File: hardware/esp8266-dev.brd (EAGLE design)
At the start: 48.3 x 48.3 mm, 31 parts, among them CON1 USBB-SOCKET

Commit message: first acceptable layout, off to review
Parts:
- added U$3: (no value), p.peter-doc:LOGO-JUSTGEEK-XXXS
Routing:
- net +3V3: track 115.8 -> 116.6 mm
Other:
- board text added: "+3V3"
- board text added: "0"
- board text added: "16"
- board text added: "2"
- board text added: "GND"
- board text added: "ISP 3v3"
- board text added: "RX"
- board text added: "TX"
- board text added: "github.com/JustgeekDE/ESP8266-devBoard"
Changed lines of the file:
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@@
 <setting verticaltext="up"/>
 </settings>
-<grid distance="0.05" unitdist="inch" unit="mil" style="lines" multiple="1" display="yes" altdistance="10" altunitdist="mil" altunit="mil"/>
+<grid distance="10" unitdist="mil" unit="mil" style="lines" multiple="1" display="yes" altdistance="5" altunitdist="mil" altunit="mil"/>
 <layers>
 <layer number="1" name="Top" color="4" fill="1" visible="no" active="yes"/>
@@
 <layer number="19" name="Unrouted" color="6" fill="1" visible="no" active="yes"/>
 <layer number="20" name="Dimension" color="15" fill="1" visible="yes" active="yes"/>
-<layer number="21" name="tPlace" color="7" fill="1" visible="yes" active="yes"/>
-<layer number="22" name="bPlace" color="7" fill="1" visible="no" active="yes"/>
+<layer number="21" name="tPlace" color="7" fill="1" visible="no" active="yes"/>
+<layer number="22" name="bPlace" color="7" fill="1" visible="yes" active="yes"/>
 <layer number="23" name="tOrigins" color="15" fill="1" visible="no" active="yes"/>
-<layer number="24" name="bOrigins" color="15" fill="1" visible="no" active="yes"/>
-<layer number="25" name="tNames" color="7" fill="1" visible="yes" active="yes"/>
-<layer number="26" name="bNames" color="7" fill="1" visible="no" active="yes"/>
-<layer number="27" name="tValues" color="7" fill="1" visible="yes" active="yes"/>
-<layer number="28" name="bValues" color="7" fill="1" visible="no" active="yes"/>
-<layer number="29" name="tStop" color="7" fill="3" visible="yes" active="yes"/>
-<layer number="30" name="bStop" color="7" fill="6" visible="no" active="yes"/>
+<layer number="24" name="bOrigins" color="15" fill="1" visible="yes" active="yes"/>
+<layer number="25" name="tNames" color="7" fill="1" visible="no" active="yes"/>
+<layer number="26" name="bNames" color="7" fill="1" visible="yes" active="yes"/>
+<layer number="27" name="tValues" color="7" fill="1" visible="no" active="yes"/>
+<layer number="28" name="bValues" color="7" fill="1" visible="yes" active="yes"/>
+<layer number="29" name="tStop" color="7" fill="3" visible="no" active="yes"/>
+<layer number="30" name="bStop" color="7" fill="6" visible="yes" active="yes"/>
 <layer number="31" name="tCream" color="7" fill="4" visible="no" active="yes"/>
 <layer number="32" name="bCream" color="7" fill="5" visible="no" active="yes"/>
@@
 <layer number="110" name="fp0" color="7" fill="1" visible="no" active="yes"/>
 <layer number="116" name="Patch_BOT" color="9" fill="4" visible="no" active="yes"/>
-<layer number="121" name="_tsilk" color="7" fill="1" visible="yes" active="yes"/>
-<layer number="122" name="_bsilk" color="7" fill="1" visible="no" active="yes"/>
+<layer number="121" name="_tsilk" color="7" fill="1" visible="no" active="yes"/>
+<layer number="122" name="_bsilk" color="7" fill="1" visible="yes" active="yes"/>
 <layer number="123" name="tTestmark" color="7" fill="1" visible="no" active="yes"/>
 <layer number="124" name="bTestmark" color="7" fill="1" visible="no" active="yes"/>
@@
 <wire x1="48.26" y1="3.81" x2="48.26" y2="5.08" width="0" layer="20"/>
 <wire x1="46.99" y1="49.53" x2="48.26" y2="48.26" width="0" layer="20" curve="-90"/>
+<text x="31.75" y="45.72" size="1.27" layer="21" font="vector" ratio="12" align="center-left">+3V3</text>
+<text x="31.75" y="43.18" size="1.27" layer="21" font="vector" ratio="12" align="center-left">RX</text>
+<text x="31.75" y="40.64" size="1.27" layer="21" font="vector" ratio="12" align="center-left">TX</text>
+<text x="31.75" y="38.1" size="1.27" layer="21" font="vector" ratio="12" align="center-left">16</text>
+<text x="31.75" y="35.56" size="1.27" layer="21" font="vector" ratio="12" align="center-left">2</text>
+<text x="31.75" y="33.02" size="1.27" layer="21" font="vector" ratio="12" align="center-left">0</text>
+<text x="31.75" y="30.48" size="1.27" layer="21" font="vector" ratio="12" align="center-left">GND</text>
+<wire x1="11.303" y1="45.72" x2="11.557" y2="45.72" width="0.508" layer="21"/>
+<wire x1="13.843" y1="45.72" x2="14.097" y2="45.72" width="0.508" layer="21"/>
+<wire x1="16.383" y1="45.72" x2="16.637" y2="45.72" width="0.508" layer="21"/>
+<wire x1="18.923" y1="45.72" x2="19.177" y2="45.72" width="0.508" layer="21"/>
+<wire x1="21.463" y1="45.72" x2="21.717" y2="45.72" width="0.508" layer="21"/>
+<wire x1="24.003" y1="45.72" x2="24.257" y2="45.72" width="0.508" layer="21"/>
+<wire x1="26.543" y1="45.72" x2="26.797" y2="45.72" width="0.508" layer="21"/>
+<wire x1="29.083" y1="45.72" x2="29.337" y2="45.72" width="0.508" layer="21"/>
+<wire x1="26.543" y1="27.94" x2="26.797" y2="27.94" width="0.508" layer="21"/>
+<wire x1="24.003" y1="27.94" x2="24.257" y2="27.94" width="0.508" layer="21"/>
+<wire x1="21.463" y1="27.94" x2="21.717" y2="27.94" width="0.508" layer="21"/>
+<wire x1="18.923" y1="27.94" x2="19.177" y2="27.94" width="0.508" layer="21"/>
+<wire x1="16.383" y1="27.94" x2="16.637" y2="27.94" width="0.508" layer="21"/>
+<wire x1="13.843" y1="27.94" x2="14.097" y2="27.94" width="0.508" layer="21"/>
+<wire x1="11.303" y1="27.94" x2="11.557" y2="27.94" width="0.508" layer="21"/>
+<wire x1="8.763" y1="27.94" x2="9.017" y2="27.94" width="0.508" layer="21"/>
+<wire x1="6.223" y1="27.94" x2="6.477" y2="27.94" width="0.508" layer="21"/>
+<wire x1="3.683" y1="27.94" x2="3.937" y2="27.94" width="0.508" layer="21"/>
+<wire x1="29.21" y1="27.94" x2="30.48" y2="29.21" width="0.508" layer="21" curve="90"/>
+<wire x1="31.115" y1="22.225" x2="47.625" y2="22.225" width="0.508" layer="21" style="shortdash"/>
+<wire x1="30.988" y1="22.225" x2="47.498" y2="22.225" width="0.508" layer="22" style="shortdash"/>
+<text x="37.592" y="15.748" size="1.016" layer="21" font="vector" ratio="12" rot="SR0" align="center">+3V3</text>
+<text x="31.496" y="17.78" size="1.016" layer="21" font="vector" ratio="12" align="center-right">GND</text>
+<text x="40.64" y="16.256" size="1.016" layer="21" font="vector" ratio="12" rot="SR270" align="center-left">TX</text>
+<text x="43.18" y="16.256" size="1.016" layer="21" font="vector" ratio="12" rot="SR270" align="center-left">RX</text>
+<text x="31.496" y="26.67" size="1.016" layer="21" font="vector" ratio="12" align="center-right">GND</text>
+<text x="37.338" y="28.702" size="1.016" layer="21" font="vector" ratio="12" rot="SR0" align="center">+3V3</text>
+<text x="40.64" y="28.702" size="1.016" layer="21" font="vector" ratio="12" rot="SR0" align="center">TX</text>
+<text x="43.18" y="28.702" size="1.016" layer="21" font="vector" ratio="12" rot="SR0" align="center">RX</text>
+<text x="33.02" y="8.636" size="1.016" layer="22" font="vector" ratio="12" rot="MR0" align="center">ISP
+3v3</text>
+<text x="20.32" y="48.006" size="1.016" layer="22" font="vector" ratio="12" rot="MR0" align="center">github.com/JustgeekDE/ESP8266-devBoard</text>
 </plain>
 <attributes>
@@
 <attribute name="VALUE" x="34.29" y="7.62" size="1.27" layer="27" font="vector" ratio="12" rot="R270" align="center"/>
 </element>
-<element name="SJ1" library="jumper" package="SJ" value="" x="33.02" y="5.08" rot="MR90"/>
+<element name="SJ1" library="jumper" package="SJ" value="" x="33.02" y="5.08" smashed="yes" rot="MR90">
+<attribute name="VALUE" x="33.02" y="5.4801" size="0.02" layer="28" rot="MR90"/>
+</element>
 <element name="CON1" library="p.peter-connectors" package="PN61729-S" value="USBB-SOCKET" x="3.81" y="10.16" smashed="yes" rot="R270"/>
 <element name="RF1" library="p.peter-periphery" package="ESP8266-ESP-01-NOSILK" value="" x="44.45" y="34.29" smashed="yes" rot="R180">
@@
 </element>
 <element name="R4" library="rcl" package="0204/7" value="10k" x="39.37" y="34.29" smashed="yes" rot="R90">
-<attribute name="NAME" x="40.8686" y="30.988" size="1.016" layer="25" font="vector" ratio="12" rot="R90" align="center"/>
+<attribute name="NAME" x="39.3446" y="40.132" size="1.016" layer="25" font="vector" ratio="12" rot="R90" align="center"/>
 <attribute name="VALUE" x="39.3446" y="33.6804" size="1.27" layer="27" font="vector" ratio="12" rot="R90" align="center"/>
 </element>
 <element name="R6" library="rcl" package="0204/7" value="10k" x="36.83" y="34.29" smashed="yes" rot="R90">
-<attribute name="NAME" x="34.7726" y="30.988" size="1.016" layer="25" font="vector" ratio="12" rot="R90" align="center"/>
+<attribute name="NAME" x="36.8046" y="40.132" size="1.016" layer="25" font="vector" ratio="12" rot="R90" align="center"/>
 <attribute name="VALUE" x="36.8046" y="33.6804" size="1.27" layer="27" font="vector" ratio="12" rot="R90" align="center"/>
 </element>
@@
 <element name="CON10" library="p.peter-connectors" package="PINHEADER-100MIL-1X7-NOSILK" value="" x="30.48" y="38.1" smashed="yes" rot="R270"/>
 <element name="CON3" library="p.peter-connectors" package="PINHEADER-100MIL-1X8-NOSILK" value="" x="19.05" y="43.18" smashed="yes"/>
+<element name="U$3" library="p.peter-doc" package="LOGO-JUSTGEEK-XXXS" value="" x="43.434" y="45.974" rot="MR0"/>
 </elements>
 <signals>
@@
 <wire x1="38.1" y1="17.78" x2="38.1" y2="26.67" width="0.508" layer="1"/>
 <wire x1="36.83" y1="11.43" x2="34.29" y2="11.43" width="0.508" layer="1"/>
-<wire x1="34.29" y1="11.43" x2="33.02" y2="10.16" width="0.508" layer="1"/>
-<wire x1="33.02" y1="10.16" x2="33.02" y2="9.144" width="0.508" layer="1"/>
-<via x="33.02" y="9.144" extent="1-16" drill="0.508"/>
-<wire x1="33.02" y1="9.144" x2="33.02" y2="5.842" width="0.508" layer="16"/>
+<wire x1="34.29" y1="11.43" x2="33.02" y2="11.43" width="0.508" layer="1"/>
+<via x="33.02" y="11.43" extent="1-16" drill="0.508"/>
+<wire x1="33.02" y1="11.43" x2="33.02" y2="5.842" width="0.508" layer="16"/>
 <contactref element="RF1" pad="VCC"/>
 <contactref element="R4" pad="2"/>
@@
 </board>
 </drawing>
+<compatibility>
+<note version="6.3" minversion="6.2.2" severity="warning">
+Since Version 6.2.2 text objects can contain more than one line,
+which will not be processed correctly with this version.
+</note>
+</compatibility>
 </eagle>

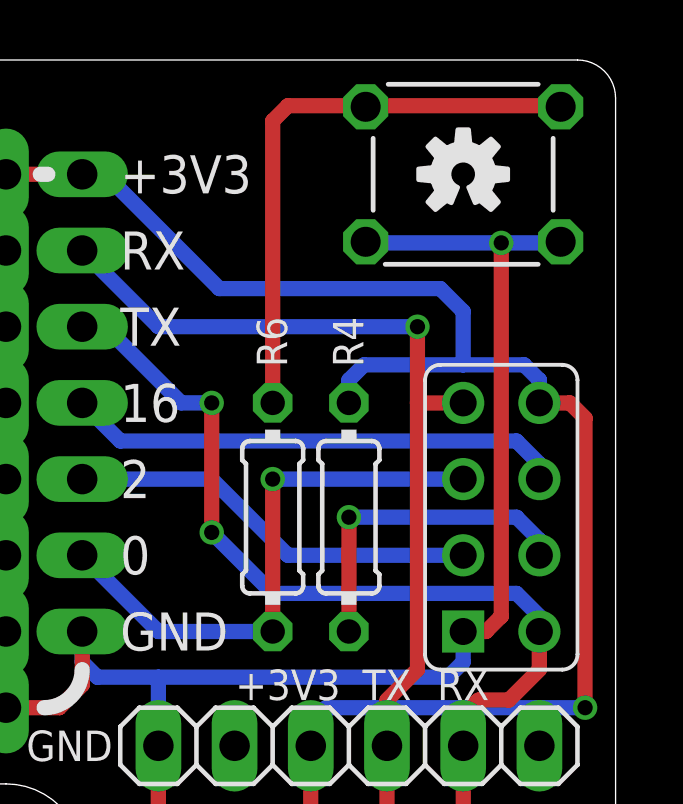
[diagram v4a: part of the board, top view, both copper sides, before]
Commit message: Added more silkscreen
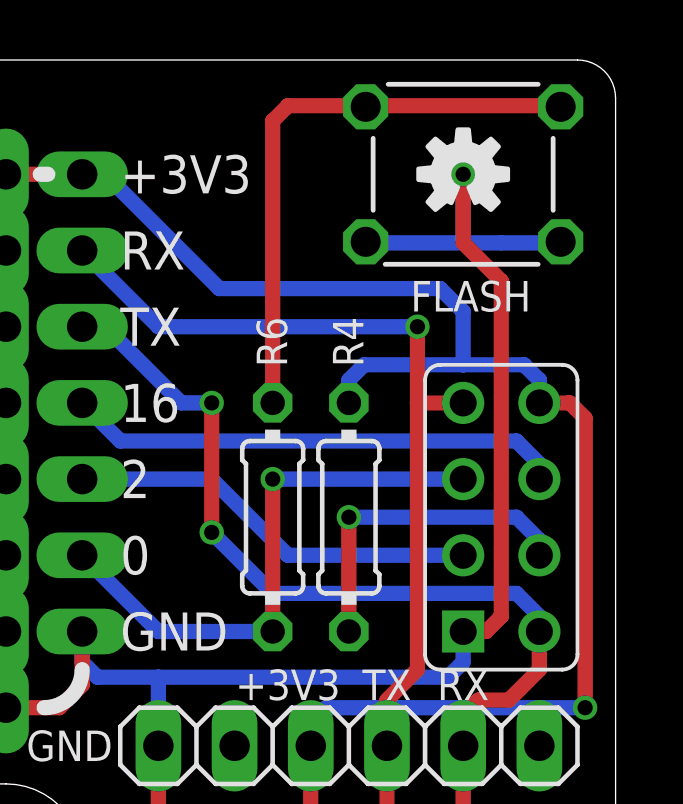
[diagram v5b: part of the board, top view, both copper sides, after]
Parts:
- moved U$3 9.99 mm to (33.5, 44.7), turned to 90 degrees
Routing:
- net GND: track 162.5 -> 167.6 mm
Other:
- board text added: "ESP 8266 dev board v0.1"
- board text added: "FLASH"
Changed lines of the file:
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@@
 <text x="33.02" y="8.636" size="1.016" layer="22" font="vector" ratio="12" rot="MR0" align="center">ISP
 3v3</text>
-<text x="20.32" y="48.006" size="1.016" layer="22" font="vector" ratio="12" rot="MR0" align="center">github.com/JustgeekDE/ESP8266-devBoard</text>
+<text x="18.288" y="48.26" size="1.016" layer="22" font="vector" ratio="12" rot="MR0" align="center">github.com/JustgeekDE/ESP8266-devBoard</text>
+<text x="43.434" y="41.656" size="1.016" layer="21" font="vector" ratio="12" rot="SR0" align="center">FLASH</text>
+<text x="34.29" y="47.498" size="1.016" layer="22" font="vector" ratio="12" rot="MR270" align="top-left">ESP 8266
+dev board
+v0.1</text>
 </plain>
 <attributes>
@@
 <element name="CON10" library="p.peter-connectors" package="PINHEADER-100MIL-1X7-NOSILK" value="" x="30.48" y="38.1" smashed="yes" rot="R270"/>
 <element name="CON3" library="p.peter-connectors" package="PINHEADER-100MIL-1X8-NOSILK" value="" x="19.05" y="43.18" smashed="yes"/>
-<element name="U$3" library="p.peter-doc" package="LOGO-JUSTGEEK-XXXS" value="" x="43.434" y="45.974" rot="MR0"/>
+<element name="U$3" library="p.peter-doc" package="LOGO-JUSTGEEK-XXXS" value="" x="33.528" y="44.704" rot="MR90"/>
 </elements>
 <signals>
@@
 <wire x1="43.18" y1="30.48" x2="43.942" y2="30.48" width="0.508" layer="1"/>
 <wire x1="43.942" y1="30.48" x2="44.45" y2="30.988" width="0.508" layer="1"/>
-<wire x1="44.45" y1="30.988" x2="44.45" y2="43.434" width="0.508" layer="1"/>
+<wire x1="44.45" y1="30.988" x2="44.45" y2="42.164" width="0.508" layer="1"/>
 <wire x1="39.93" y1="43.47" x2="39.878" y2="43.434" width="0.508" layer="16"/>
-<wire x1="39.878" y1="43.434" x2="44.45" y2="43.434" width="0.508" layer="16"/>
+<wire x1="39.878" y1="43.434" x2="43.18" y2="43.434" width="0.508" layer="16"/>
+<wire x1="43.18" y1="43.434" x2="44.45" y2="43.434" width="0.508" layer="16"/>
 <wire x1="44.45" y1="43.434" x2="46.482" y2="43.434" width="0.508" layer="16"/>
 <wire x1="46.482" y1="43.434" x2="46.43" y2="43.47" width="0.508" layer="16"/>
-<via x="44.45" y="43.434" extent="1-16" drill="0.508"/>
 <contactref element="IC2" pad="2"/>
 <wire x1="13.97" y1="3.81" x2="14.224" y2="3.556" width="0.508" layer="1"/>
@@
 <wire x1="30.988" y1="28.956" x2="30.48" y2="29.464" width="0.508" layer="16"/>
 <wire x1="30.48" y1="29.464" x2="30.48" y2="30.48" width="0.508" layer="16"/>
+<wire x1="44.45" y1="42.164" x2="43.18" y2="43.434" width="0.508" layer="1"/>
+<wire x1="43.18" y1="43.434" x2="43.18" y2="45.72" width="0.508" layer="1"/>
+<via x="43.18" y="45.72" extent="1-16" drill="0.508"/>
+<wire x1="43.18" y1="45.72" x2="43.18" y2="43.434" width="0.508" layer="16"/>
 </signal>
 <signal name="N$1">

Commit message: Further cleanup
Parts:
- IC2: value (none) -> 3V3
- R1, R2: value 27 -> 68
- R3: value 1.2k -> 1.5k
- moved R2 2.54 mm to (15.2, 8.89)
- moved R3 2.54 mm to (15.2, 11.4)
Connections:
- net +3V3: now also R3.2
- net +5V: no longer R3.2
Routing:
- net +3V3: track 116.6 -> 123.8 mm
- net +5V: track 12.0 -> 8.15 mm
- net N$1: track 11.2 -> 10.2 mm
